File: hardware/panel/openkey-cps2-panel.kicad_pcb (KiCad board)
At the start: 2 copper layers, 124 x 108.8 mm, 198 parts, among them CN10 Conn_01x06, CN11 Conn_01x06, CN12 Conn_01x06, CN13 Conn_01x06, CN14 Conn_01x06, CN15 Conn_01x06, CN16 Conn_01x06, CN17 Conn_01x06, CN9 Conn_01x06, J1 VCC Pad, J10 VCC, J11 GND, J12 J5 / UDPI, J13 VCC Pad, J14 CN2, J15 GND Pad, J16 VCC, J17 GND, J18 J5 / UDPI, J19 VCC Pad, J2 CN2, J20 CN2, J21 GND Pad, J22 VCC, J23 GND, J24 J5 / UDPI, J25 VCC Pad, J26 CN2, J27 GND Pad, J28 VCC, J29 GND, J3 GND Pad, J30 J5 / UDPI, J31 VCC Pad, J32 CN2, J33 GND Pad, J34 VCC, J35 GND, J36 J5 / UDPI, J37 VCC Pad, J38 CN2, J39 GND Pad, J4 VCC, J40 VCC, J41 GND, J42 J5 / UDPI, J43 VCC Pad, J44 CN2, J45 GND Pad, J46 VCC, J47 GND, J48 J5 / UDPI, J49 VCC Pad, J5 GND, J50 CN2, J51 GND Pad, J52 VCC, J53 GND, J54 J5 / UDPI, J6 J5 / UDPI, J7 VCC Pad, J8 CN2, J9 GND Pad, U1 ATtinyxx4, U2 ATtinyxx4, U3 ATtinyxx4, U4 ATtinyxx4, U5 ATtinyxx4, U6 ATtinyxx4, U7 ATtinyxx4, U8 ATtinyxx4, U9 ATtinyxx4

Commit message: HW: bypass cap value typo'd as 100uf when it should be 100nf
Thanks for hatmoose for pointing out the typo
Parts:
- C1, C2, C3, C4, C5, C6, C7, C8, C9: value 100uf -> 100nf
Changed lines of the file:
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@@
     )
   )
-  (property "REV" "2022-12-17")
+  (property "REV" "2023-01-03")
   (net 0 "")
   (net 1 "VCC")
@@
       (effects (font (size 0.7 0.7) (thickness 0.12)))
     )
-    (fp_text value "100uf" (at -2.5 0) (layer "F.SilkS")
+    (fp_text value "100nf" (at -2.5 0) (layer "F.SilkS")
       (effects (font (size 0.7 0.7) (thickness 0.12)))
     )
@@
       (effects (font (size 0.7 0.7) (thickness 0.12)))
     )
-    (fp_text value "100uf" (at -2.5 0) (layer "F.SilkS")
+    (fp_text value "100nf" (at -2.5 0) (layer "F.SilkS")
       (effects (font (size 0.7 0.7) (thickness 0.12)))
     )
@@
       (effects (font (size 0.7 0.7) (thickness 0.12)))
     )
-    (fp_text value "100uf" (at -2.5 0) (layer "F.SilkS")
+    (fp_text value "100nf" (at -2.5 0) (layer "F.SilkS")
       (effects (font (size 0.7 0.7) (thickness 0.12)))
     )
@@
       (effects (font (size 0.7 0.7) (thickness 0.12)))
     )
-    (fp_text value "100uf" (at -2.5 0) (layer "F.SilkS")
+    (fp_text value "100nf" (at -2.5 0) (layer "F.SilkS")
       (effects (font (size 0.7 0.7) (thickness 0.12)))
     )
@@
       (effects (font (size 0.7 0.7) (thickness 0.12)))
     )
-    (fp_text value "100uf" (at -2.5 0) (layer "F.SilkS")
+    (fp_text value "100nf" (at -2.5 0) (layer "F.SilkS")
       (effects (font (size 0.7 0.7) (thickness 0.12)))
     )
@@
       (effects (font (size 0.7 0.7) (thickness 0.12)))
     )
-    (fp_text value "100uf" (at -2.5 0) (layer "F.SilkS")
+    (fp_text value "100nf" (at -2.5 0) (layer "F.SilkS")
       (effects (font (size 0.7 0.7) (thickness 0.12)))
     )
@@
       (effects (font (size 0.7 0.7) (thickness 0.12)))
     )
-    (fp_text value "100uf" (at -2.5 0) (layer "F.SilkS")
+    (fp_text value "100nf" (at -2.5 0) (layer "F.SilkS")
       (effects (font (size 0.7 0.7) (thickness 0.12)))
     )
@@
       (effects (font (size 0.7 0.7) (thickness 0.12)))
     )
-    (fp_text value "100uf" (at -2.5 0) (layer "F.SilkS")
+    (fp_text value "100nf" (at -2.5 0) (layer "F.SilkS")
       (effects (font (size 0.7 0.7) (thickness 0.12)))
     )
@@
       (effects (font (size 0.7 0.7) (thickness 0.12)))
     )
-    (fp_text value "100uf" (at -2.5 0) (layer "F.SilkS")
+    (fp_text value "100nf" (at -2.5 0) (layer "F.SilkS")
       (effects (font (size 0.7 0.7) (thickness 0.12)))
     )

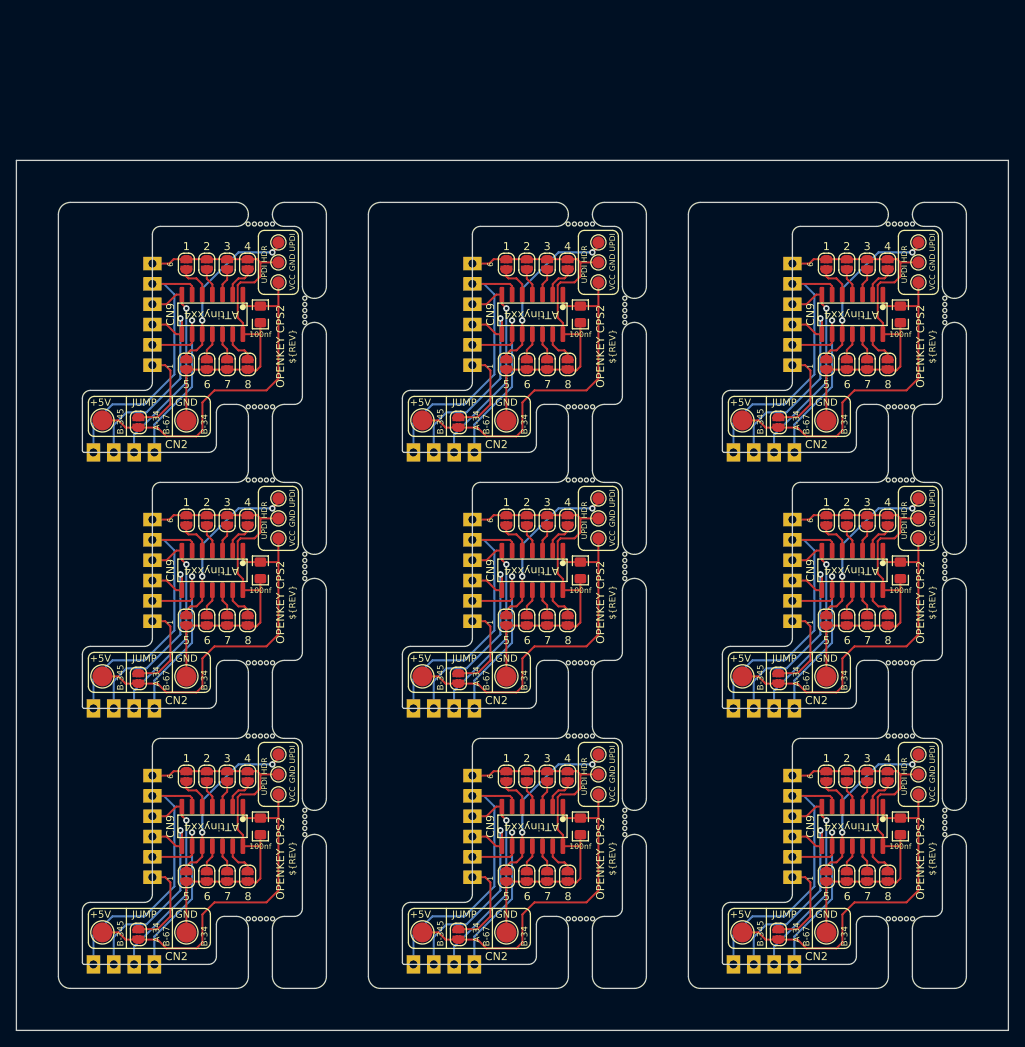
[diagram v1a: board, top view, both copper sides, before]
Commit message: panel + assembly updates
- have kikit create the panel (was done by hand before)
- have jlcpcb fabrication plugin create bom/positions files for the panel
- create PANEL.md with instructions for having jlcpcb assemble the board
- update kicad files to 10.x
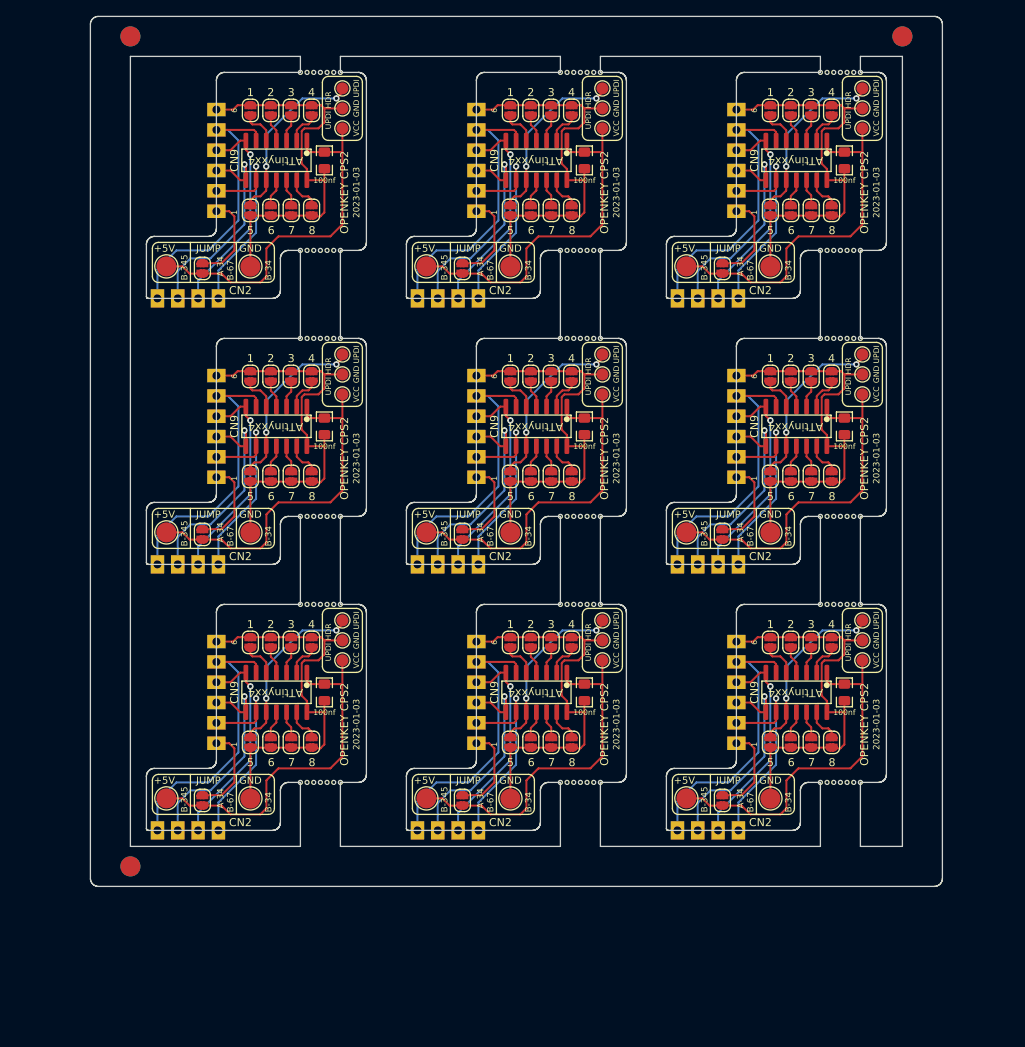
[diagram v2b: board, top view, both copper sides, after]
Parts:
- removed the C1 at (116.5, 57.2)
- removed C2, C3, C4, C5, C6, C7, C8, C9: 100nf, openkey:C_0805_2012Metric_Pad1.18x1.45mm_HandSolder
- removed CN10, CN11, CN12, CN13, CN14, CN15, CN16, CN17: Conn_01x06, Connector_PinHeader_2.54mm:PinHeader_1x06_P2.54mm_Vertical
- removed the CN9 at (103.0, 63.6)
- removed the J1 at (96.8, 70.5)
- removed J10, J16, J22, J28, J34, J40, J46, J52: VCC, TestPoint:TestPoint_Pad_D1.5mm
- removed J11, J17, J23, J29, J35, J41, J47, J53: GND, TestPoint:TestPoint_Pad_D1.5mm
- removed J12, J18, J24, J30, J36, J42, J48, J54: J5 / UDPI, TestPoint:TestPoint_Pad_D1.5mm
- removed J13, J19, J25, J31, J37, J43, J49, J7: VCC Pad, TestPoint:TestPoint_Pad_D2.5mm
- removed J14, J20, J26, J32, J38, J44, J50, J8: CN2, Connector_PinHeader_2.54mm:PinHeader_1x04_P2.54mm_Vertical
- removed J15, J21, J27, J33, J39, J45, J51, J9: GND Pad, TestPoint:TestPoint_Pad_D2.5mm
- removed the J2 at (103.2, 74.5)
- removed the J3 at (107.2, 70.5)
- removed the J4 at (118.8, 53.2)
- removed the J5 at (118.8, 50.8)
- removed the J6 at (118.8, 48.2)
- removed the JP1 at (107.2, 63.5)
- removed JP10, JP11, JP12, JP13, JP14, JP15, JP16, JP17, JP19, JP20, JP21, JP22, JP23, JP24, JP25, JP26, JP28, JP29, JP30, JP31, JP32, JP33, JP34, JP35, JP37, JP38, JP39, JP40, JP41, JP42, JP43, JP44, JP46, JP47, JP48, JP49, JP50, JP51, JP52, JP53, JP55, JP56, JP57, JP58, JP59, JP60, JP61, JP62, JP64, JP65, JP66, JP67, JP68, JP69, JP70, JP71, JP73, JP74, JP75, JP76, JP77, JP78, JP79, JP80: SolderJumper_2_Open, Jumper:SolderJumper-2_P1.3mm_Open_RoundedPad1.0x1.5mm
- removed JP18, JP27, JP36, JP45, JP54, JP63, JP72, JP81: CN9 VCC Jumper, Jumper:SolderJumper-2_P1.3mm_Open_RoundedPad1.0x1.5mm
- removed the JP2 at (109.8, 63.5)
- removed the JP3 at (112.3, 63.5)
- removed the JP4 at (114.9, 63.5)
- removed the JP5 at (114.9, 51.0)
- removed the JP6 at (112.3, 51.0)
- removed the JP7 at (109.8, 51.0)
- removed the JP8 at (107.2, 51.0)
- removed the JP9 at (101.2, 70.8)
- removed the REF** at (113.0, 58.0)
- removed REF**1, REF**2, REF**3, REF**4, REF**5, REF**6, REF**7, REF**8: OSHW-Logo_11.4x12mm_SilkScreen, Symbol:OSHW-Logo_11.4x12mm_SilkScreen
- removed the U1 at (110.5, 57.2)
- removed U2, U3, U4, U5, U6, U7, U8, U9: ATtinyxx4, openkey:SOIC-14_3.9x8.7mm_P1.27mm
- removed mouse-bite-3mm-slot1 (x3), mouse-bite-3mm-slot10, mouse-bite-3mm-slot11, mouse-bite-3mm-slot12, mouse-bite-3mm-slot13, mouse-bite-3mm-slot14, mouse-bite-3mm-slot15, mouse-bite-3mm-slot16, mouse-bite-3mm-slot17, mouse-bite-3mm-slot18, mouse-bite-3mm-slot19, mouse-bite-3mm-slot2, mouse-bite-3mm-slot20, mouse-bite-3mm-slot21, mouse-bite-3mm-slot22, mouse-bite-3mm-slot23, mouse-bite-3mm-slot24, mouse-bite-3mm-slot25, mouse-bite-3mm-slot3, mouse-bite-3mm-slot4, mouse-bite-3mm-slot5, mouse-bite-3mm-slot6, mouse-bite-3mm-slot7, mouse-bite-3mm-slot8, mouse-bite-3mm-slot9: VAL**, Panelization:mouse-bite-3mm-slot
- added C1: 100nf, openkey:C_0805_2012Metric_Pad1.18x1.45mm_HandSolder, F.Cu at (189.5, 71.2)
- added C1: 100nf, openkey:C_0805_2012Metric_Pad1.18x1.45mm_HandSolder, F.Cu at (124.5, 104.5)
- added C1: 100nf, openkey:C_0805_2012Metric_Pad1.18x1.45mm_HandSolder, F.Cu at (124.5, 71.2)
- added C1: 100nf, openkey:C_0805_2012Metric_Pad1.18x1.45mm_HandSolder, F.Cu at (189.5, 104.5)
- added C1: 100nf, openkey:C_0805_2012Metric_Pad1.18x1.45mm_HandSolder, F.Cu at (157.0, 71.2)
- added C1: 100nf, openkey:C_0805_2012Metric_Pad1.18x1.45mm_HandSolder, F.Cu at (157.0, 104.5)
- added C1: 100nf, openkey:C_0805_2012Metric_Pad1.18x1.45mm_HandSolder, F.Cu at (124.5, 38.0)
- added C1: 100nf, openkey:C_0805_2012Metric_Pad1.18x1.45mm_HandSolder, F.Cu at (157.0, 38.0)
- added C1: 100nf, openkey:C_0805_2012Metric_Pad1.18x1.45mm_HandSolder, F.Cu at (189.5, 38.0)
- added CN9: Conn_01x06, Connector_PinHeader_2.54mm:PinHeader_1x06_P2.54mm_Vertical, F.Cu at (176.0, 44.4)
- added CN9: Conn_01x06, Connector_PinHeader_2.54mm:PinHeader_1x06_P2.54mm_Vertical, F.Cu at (176.0, 77.6)
- added CN9: Conn_01x06, Connector_PinHeader_2.54mm:PinHeader_1x06_P2.54mm_Vertical, F.Cu at (143.5, 44.4)
- added CN9: Conn_01x06, Connector_PinHeader_2.54mm:PinHeader_1x06_P2.54mm_Vertical, F.Cu at (111.0, 110.8)
- added CN9: Conn_01x06, Connector_PinHeader_2.54mm:PinHeader_1x06_P2.54mm_Vertical, F.Cu at (143.5, 77.6)
- added CN9: Conn_01x06, Connector_PinHeader_2.54mm:PinHeader_1x06_P2.54mm_Vertical, F.Cu at (111.0, 44.4)
- added CN9: Conn_01x06, Connector_PinHeader_2.54mm:PinHeader_1x06_P2.54mm_Vertical, F.Cu at (143.5, 110.8)
- added CN9: Conn_01x06, Connector_PinHeader_2.54mm:PinHeader_1x06_P2.54mm_Vertical, F.Cu at (176.0, 110.8)
- added CN9: Conn_01x06, Connector_PinHeader_2.54mm:PinHeader_1x06_P2.54mm_Vertical, F.Cu at (111.0, 77.6)
- added J1: VCC Pad, TestPoint:TestPoint_Pad_D2.5mm, F.Cu at (104.8, 51.2)
- added J1: VCC Pad, TestPoint:TestPoint_Pad_D2.5mm, F.Cu at (169.8, 117.8)
- added J1: VCC Pad, TestPoint:TestPoint_Pad_D2.5mm, F.Cu at (137.2, 84.5)
- added J1: VCC Pad, TestPoint:TestPoint_Pad_D2.5mm, F.Cu at (104.8, 84.5)
- added J1: VCC Pad, TestPoint:TestPoint_Pad_D2.5mm, F.Cu at (137.2, 51.2)
- added J1: VCC Pad, TestPoint:TestPoint_Pad_D2.5mm, F.Cu at (169.8, 51.2)
- added J1: VCC Pad, TestPoint:TestPoint_Pad_D2.5mm, F.Cu at (169.8, 84.5)
- added J1: VCC Pad, TestPoint:TestPoint_Pad_D2.5mm, F.Cu at (104.8, 117.8)
- added J1: VCC Pad, TestPoint:TestPoint_Pad_D2.5mm, F.Cu at (137.2, 117.8)
- added J2: CN2, Connector_PinHeader_2.54mm:PinHeader_1x04_P2.54mm_Vertical, F.Cu at (143.8, 88.5)
- added J2: CN2, Connector_PinHeader_2.54mm:PinHeader_1x04_P2.54mm_Vertical, F.Cu at (176.2, 121.8)
- added J2: CN2, Connector_PinHeader_2.54mm:PinHeader_1x04_P2.54mm_Vertical, F.Cu at (143.8, 55.2)
- added J2: CN2, Connector_PinHeader_2.54mm:PinHeader_1x04_P2.54mm_Vertical, F.Cu at (111.2, 55.2)
- added J2: CN2, Connector_PinHeader_2.54mm:PinHeader_1x04_P2.54mm_Vertical, F.Cu at (111.2, 121.8)
- added J2: CN2, Connector_PinHeader_2.54mm:PinHeader_1x04_P2.54mm_Vertical, F.Cu at (176.2, 88.5)
- added J2: CN2, Connector_PinHeader_2.54mm:PinHeader_1x04_P2.54mm_Vertical, F.Cu at (176.2, 55.2)
- added J2: CN2, Connector_PinHeader_2.54mm:PinHeader_1x04_P2.54mm_Vertical, F.Cu at (111.2, 88.5)
- added J2: CN2, Connector_PinHeader_2.54mm:PinHeader_1x04_P2.54mm_Vertical, F.Cu at (143.8, 121.8)
- added J3: GND Pad, TestPoint:TestPoint_Pad_D2.5mm, F.Cu at (115.2, 84.5)
- added J3: GND Pad, TestPoint:TestPoint_Pad_D2.5mm, F.Cu at (115.2, 51.2)
- added J3: GND Pad, TestPoint:TestPoint_Pad_D2.5mm, F.Cu at (147.8, 84.5)
- added J3: GND Pad, TestPoint:TestPoint_Pad_D2.5mm, F.Cu at (180.2, 51.2)
- added J3: GND Pad, TestPoint:TestPoint_Pad_D2.5mm, F.Cu at (115.2, 117.8)
- added J3: GND Pad, TestPoint:TestPoint_Pad_D2.5mm, F.Cu at (147.8, 117.8)
- added J3: GND Pad, TestPoint:TestPoint_Pad_D2.5mm, F.Cu at (180.2, 117.8)
- added J3: GND Pad, TestPoint:TestPoint_Pad_D2.5mm, F.Cu at (147.8, 51.2)
- added J3: GND Pad, TestPoint:TestPoint_Pad_D2.5mm, F.Cu at (180.2, 84.5)
- added J4: VCC, TestPoint:TestPoint_Pad_D1.5mm, F.Cu at (159.2, 34.0)
- added J4: VCC, TestPoint:TestPoint_Pad_D1.5mm, F.Cu at (126.8, 100.5)
- added J4: VCC, TestPoint:TestPoint_Pad_D1.5mm, F.Cu at (126.8, 67.2)
- added J4: VCC, TestPoint:TestPoint_Pad_D1.5mm, F.Cu at (159.2, 100.5)
- added J4: VCC, TestPoint:TestPoint_Pad_D1.5mm, F.Cu at (191.8, 34.0)
- added J4: VCC, TestPoint:TestPoint_Pad_D1.5mm, F.Cu at (191.8, 100.5)
- added J4: VCC, TestPoint:TestPoint_Pad_D1.5mm, F.Cu at (191.8, 67.2)
- added J4: VCC, TestPoint:TestPoint_Pad_D1.5mm, F.Cu at (159.2, 67.2)
- added J4: VCC, TestPoint:TestPoint_Pad_D1.5mm, F.Cu at (126.8, 34.0)
- added J5: GND, TestPoint:TestPoint_Pad_D1.5mm, F.Cu at (126.8, 64.8)
- added J5: GND, TestPoint:TestPoint_Pad_D1.5mm, F.Cu at (126.8, 98.0)
- added J5: GND, TestPoint:TestPoint_Pad_D1.5mm, F.Cu at (191.8, 31.5)
- added J5: GND, TestPoint:TestPoint_Pad_D1.5mm, F.Cu at (191.8, 98.0)
- added J5: GND, TestPoint:TestPoint_Pad_D1.5mm, F.Cu at (159.2, 64.8)
- added J5: GND, TestPoint:TestPoint_Pad_D1.5mm, F.Cu at (159.2, 31.5)
- added J5: GND, TestPoint:TestPoint_Pad_D1.5mm, F.Cu at (126.8, 31.5)
- added J5: GND, TestPoint:TestPoint_Pad_D1.5mm, F.Cu at (159.2, 98.0)
- added J5: GND, TestPoint:TestPoint_Pad_D1.5mm, F.Cu at (191.8, 64.8)
- added J6: J5 / UDPI, TestPoint:TestPoint_Pad_D1.5mm, F.Cu at (191.8, 29.0)
- added J6: J5 / UDPI, TestPoint:TestPoint_Pad_D1.5mm, F.Cu at (159.2, 29.0)
- added J6: J5 / UDPI, TestPoint:TestPoint_Pad_D1.5mm, F.Cu at (126.8, 62.2)
- added J6: J5 / UDPI, TestPoint:TestPoint_Pad_D1.5mm, F.Cu at (191.8, 62.2)
- added J6: J5 / UDPI, TestPoint:TestPoint_Pad_D1.5mm, F.Cu at (126.8, 29.0)
- added J6: J5 / UDPI, TestPoint:TestPoint_Pad_D1.5mm, F.Cu at (159.2, 62.2)
- added J6: J5 / UDPI, TestPoint:TestPoint_Pad_D1.5mm, F.Cu at (126.8, 95.5)
- added J6: J5 / UDPI, TestPoint:TestPoint_Pad_D1.5mm, F.Cu at (191.8, 95.5)
- added J6: J5 / UDPI, TestPoint:TestPoint_Pad_D1.5mm, F.Cu at (159.2, 95.5)
- added JP1: SolderJumper_2_Open, Jumper:SolderJumper-2_P1.3mm_Open_RoundedPad1.0x1.5mm, F.Cu at (115.2, 110.8)
- added JP1: SolderJumper_2_Open, Jumper:SolderJumper-2_P1.3mm_Open_RoundedPad1.0x1.5mm, F.Cu at (147.8, 77.5)
- added JP1: SolderJumper_2_Open, Jumper:SolderJumper-2_P1.3mm_Open_RoundedPad1.0x1.5mm, F.Cu at (147.8, 110.8)
- added JP1: SolderJumper_2_Open, Jumper:SolderJumper-2_P1.3mm_Open_RoundedPad1.0x1.5mm, F.Cu at (180.2, 44.2)
- added JP1: SolderJumper_2_Open, Jumper:SolderJumper-2_P1.3mm_Open_RoundedPad1.0x1.5mm, F.Cu at (115.2, 44.2)
- added JP1: SolderJumper_2_Open, Jumper:SolderJumper-2_P1.3mm_Open_RoundedPad1.0x1.5mm, F.Cu at (115.2, 77.5)
- added JP1: SolderJumper_2_Open, Jumper:SolderJumper-2_P1.3mm_Open_RoundedPad1.0x1.5mm, F.Cu at (180.2, 77.5)
- added JP1: SolderJumper_2_Open, Jumper:SolderJumper-2_P1.3mm_Open_RoundedPad1.0x1.5mm, F.Cu at (147.8, 44.2)
- added JP1: SolderJumper_2_Open, Jumper:SolderJumper-2_P1.3mm_Open_RoundedPad1.0x1.5mm, F.Cu at (180.2, 110.8)
- added JP2: SolderJumper_2_Open, Jumper:SolderJumper-2_P1.3mm_Open_RoundedPad1.0x1.5mm, F.Cu at (150.3, 110.8)
- added JP2: SolderJumper_2_Open, Jumper:SolderJumper-2_P1.3mm_Open_RoundedPad1.0x1.5mm, F.Cu at (182.8, 77.5)
- added JP2: SolderJumper_2_Open, Jumper:SolderJumper-2_P1.3mm_Open_RoundedPad1.0x1.5mm, F.Cu at (150.3, 77.5)
- added JP2: SolderJumper_2_Open, Jumper:SolderJumper-2_P1.3mm_Open_RoundedPad1.0x1.5mm, F.Cu at (182.8, 110.8)
- added JP2: SolderJumper_2_Open, Jumper:SolderJumper-2_P1.3mm_Open_RoundedPad1.0x1.5mm, F.Cu at (150.3, 44.2)
- added JP2: SolderJumper_2_Open, Jumper:SolderJumper-2_P1.3mm_Open_RoundedPad1.0x1.5mm, F.Cu at (117.8, 77.5)
- added JP2: SolderJumper_2_Open, Jumper:SolderJumper-2_P1.3mm_Open_RoundedPad1.0x1.5mm, F.Cu at (182.8, 44.2)
- added JP2: SolderJumper_2_Open, Jumper:SolderJumper-2_P1.3mm_Open_RoundedPad1.0x1.5mm, F.Cu at (117.8, 110.8)
- added JP2: SolderJumper_2_Open, Jumper:SolderJumper-2_P1.3mm_Open_RoundedPad1.0x1.5mm, F.Cu at (117.8, 44.2)
- added JP3: SolderJumper_2_Open, Jumper:SolderJumper-2_P1.3mm_Open_RoundedPad1.0x1.5mm, F.Cu at (120.3, 110.8)
- added JP3: SolderJumper_2_Open, Jumper:SolderJumper-2_P1.3mm_Open_RoundedPad1.0x1.5mm, F.Cu at (185.3, 77.5)
- added JP3: SolderJumper_2_Open, Jumper:SolderJumper-2_P1.3mm_Open_RoundedPad1.0x1.5mm, F.Cu at (120.3, 44.2)
- added JP3: SolderJumper_2_Open, Jumper:SolderJumper-2_P1.3mm_Open_RoundedPad1.0x1.5mm, F.Cu at (152.8, 77.5)
- added JP3: SolderJumper_2_Open, Jumper:SolderJumper-2_P1.3mm_Open_RoundedPad1.0x1.5mm, F.Cu at (152.8, 110.8)
- added JP3: SolderJumper_2_Open, Jumper:SolderJumper-2_P1.3mm_Open_RoundedPad1.0x1.5mm, F.Cu at (152.8, 44.2)
- added JP3: SolderJumper_2_Open, Jumper:SolderJumper-2_P1.3mm_Open_RoundedPad1.0x1.5mm, F.Cu at (120.3, 77.5)
- added JP3: SolderJumper_2_Open, Jumper:SolderJumper-2_P1.3mm_Open_RoundedPad1.0x1.5mm, F.Cu at (185.3, 110.8)
- added JP3: SolderJumper_2_Open, Jumper:SolderJumper-2_P1.3mm_Open_RoundedPad1.0x1.5mm, F.Cu at (185.3, 44.2)
- added JP4: SolderJumper_2_Open, Jumper:SolderJumper-2_P1.3mm_Open_RoundedPad1.0x1.5mm, F.Cu at (155.4, 44.2)
- added JP4: SolderJumper_2_Open, Jumper:SolderJumper-2_P1.3mm_Open_RoundedPad1.0x1.5mm, F.Cu at (187.9, 110.8)
- added JP4: SolderJumper_2_Open, Jumper:SolderJumper-2_P1.3mm_Open_RoundedPad1.0x1.5mm, F.Cu at (155.4, 77.5)
- added JP4: SolderJumper_2_Open, Jumper:SolderJumper-2_P1.3mm_Open_RoundedPad1.0x1.5mm, F.Cu at (122.9, 110.8)
- added JP4: SolderJumper_2_Open, Jumper:SolderJumper-2_P1.3mm_Open_RoundedPad1.0x1.5mm, F.Cu at (122.9, 44.2)
- added JP4: SolderJumper_2_Open, Jumper:SolderJumper-2_P1.3mm_Open_RoundedPad1.0x1.5mm, F.Cu at (155.4, 110.8)
- added JP4: SolderJumper_2_Open, Jumper:SolderJumper-2_P1.3mm_Open_RoundedPad1.0x1.5mm, F.Cu at (187.9, 44.2)
- added JP4: SolderJumper_2_Open, Jumper:SolderJumper-2_P1.3mm_Open_RoundedPad1.0x1.5mm, F.Cu at (122.9, 77.5)
- added JP4: SolderJumper_2_Open, Jumper:SolderJumper-2_P1.3mm_Open_RoundedPad1.0x1.5mm, F.Cu at (187.9, 77.5)
- added JP5: SolderJumper_2_Open, Jumper:SolderJumper-2_P1.3mm_Open_RoundedPad1.0x1.5mm, F.Cu at (122.9, 65.0)
- added JP5: SolderJumper_2_Open, Jumper:SolderJumper-2_P1.3mm_Open_RoundedPad1.0x1.5mm, F.Cu at (187.9, 98.2)
- added JP5: SolderJumper_2_Open, Jumper:SolderJumper-2_P1.3mm_Open_RoundedPad1.0x1.5mm, F.Cu at (155.4, 98.2)
- added JP5: SolderJumper_2_Open, Jumper:SolderJumper-2_P1.3mm_Open_RoundedPad1.0x1.5mm, F.Cu at (187.9, 65.0)
- added JP5: SolderJumper_2_Open, Jumper:SolderJumper-2_P1.3mm_Open_RoundedPad1.0x1.5mm, F.Cu at (122.9, 31.8)
- added JP5: SolderJumper_2_Open, Jumper:SolderJumper-2_P1.3mm_Open_RoundedPad1.0x1.5mm, F.Cu at (155.4, 65.0)
- added JP5: SolderJumper_2_Open, Jumper:SolderJumper-2_P1.3mm_Open_RoundedPad1.0x1.5mm, F.Cu at (187.9, 31.8)
- added JP5: SolderJumper_2_Open, Jumper:SolderJumper-2_P1.3mm_Open_RoundedPad1.0x1.5mm, F.Cu at (122.9, 98.2)
- added JP5: SolderJumper_2_Open, Jumper:SolderJumper-2_P1.3mm_Open_RoundedPad1.0x1.5mm, F.Cu at (155.4, 31.8)
- added JP6: SolderJumper_2_Open, Jumper:SolderJumper-2_P1.3mm_Open_RoundedPad1.0x1.5mm, F.Cu at (185.3, 98.2)
- added JP6: SolderJumper_2_Open, Jumper:SolderJumper-2_P1.3mm_Open_RoundedPad1.0x1.5mm, F.Cu at (152.8, 31.8)
- added JP6: SolderJumper_2_Open, Jumper:SolderJumper-2_P1.3mm_Open_RoundedPad1.0x1.5mm, F.Cu at (185.3, 31.8)
- added JP6: SolderJumper_2_Open, Jumper:SolderJumper-2_P1.3mm_Open_RoundedPad1.0x1.5mm, F.Cu at (120.3, 65.0)
- added JP6: SolderJumper_2_Open, Jumper:SolderJumper-2_P1.3mm_Open_RoundedPad1.0x1.5mm, F.Cu at (185.3, 65.0)
- added JP6: SolderJumper_2_Open, Jumper:SolderJumper-2_P1.3mm_Open_RoundedPad1.0x1.5mm, F.Cu at (152.8, 98.2)
- added JP6: SolderJumper_2_Open, Jumper:SolderJumper-2_P1.3mm_Open_RoundedPad1.0x1.5mm, F.Cu at (120.3, 31.8)
- added JP6: SolderJumper_2_Open, Jumper:SolderJumper-2_P1.3mm_Open_RoundedPad1.0x1.5mm, F.Cu at (120.3, 98.2)
- added JP6: SolderJumper_2_Open, Jumper:SolderJumper-2_P1.3mm_Open_RoundedPad1.0x1.5mm, F.Cu at (152.8, 65.0)
- added JP7: SolderJumper_2_Open, Jumper:SolderJumper-2_P1.3mm_Open_RoundedPad1.0x1.5mm, F.Cu at (182.8, 98.2)
- added JP7: SolderJumper_2_Open, Jumper:SolderJumper-2_P1.3mm_Open_RoundedPad1.0x1.5mm, F.Cu at (150.3, 98.2)
- added JP7: SolderJumper_2_Open, Jumper:SolderJumper-2_P1.3mm_Open_RoundedPad1.0x1.5mm, F.Cu at (182.8, 65.0)
- added JP7: SolderJumper_2_Open, Jumper:SolderJumper-2_P1.3mm_Open_RoundedPad1.0x1.5mm, F.Cu at (150.3, 65.0)
- added JP7: SolderJumper_2_Open, Jumper:SolderJumper-2_P1.3mm_Open_RoundedPad1.0x1.5mm, F.Cu at (182.8, 31.8)
- added JP7: SolderJumper_2_Open, Jumper:SolderJumper-2_P1.3mm_Open_RoundedPad1.0x1.5mm, F.Cu at (117.8, 31.8)
- added JP7: SolderJumper_2_Open, Jumper:SolderJumper-2_P1.3mm_Open_RoundedPad1.0x1.5mm, F.Cu at (117.8, 98.2)
- added JP7: SolderJumper_2_Open, Jumper:SolderJumper-2_P1.3mm_Open_RoundedPad1.0x1.5mm, F.Cu at (150.3, 31.8)
- added JP7: SolderJumper_2_Open, Jumper:SolderJumper-2_P1.3mm_Open_RoundedPad1.0x1.5mm, F.Cu at (117.8, 65.0)
- added JP8: SolderJumper_2_Open, Jumper:SolderJumper-2_P1.3mm_Open_RoundedPad1.0x1.5mm, F.Cu at (147.8, 65.0)
- added JP8: SolderJumper_2_Open, Jumper:SolderJumper-2_P1.3mm_Open_RoundedPad1.0x1.5mm, F.Cu at (180.2, 65.0)
- added JP8: SolderJumper_2_Open, Jumper:SolderJumper-2_P1.3mm_Open_RoundedPad1.0x1.5mm, F.Cu at (115.2, 98.2)
- added JP8: SolderJumper_2_Open, Jumper:SolderJumper-2_P1.3mm_Open_RoundedPad1.0x1.5mm, F.Cu at (180.2, 31.8)
- added JP8: SolderJumper_2_Open, Jumper:SolderJumper-2_P1.3mm_Open_RoundedPad1.0x1.5mm, F.Cu at (115.2, 65.0)
- added JP8: SolderJumper_2_Open, Jumper:SolderJumper-2_P1.3mm_Open_RoundedPad1.0x1.5mm, F.Cu at (147.8, 98.2)
- added JP8: SolderJumper_2_Open, Jumper:SolderJumper-2_P1.3mm_Open_RoundedPad1.0x1.5mm, F.Cu at (180.2, 98.2)
- added JP8: SolderJumper_2_Open, Jumper:SolderJumper-2_P1.3mm_Open_RoundedPad1.0x1.5mm, F.Cu at (115.2, 31.8)
- added JP8: SolderJumper_2_Open, Jumper:SolderJumper-2_P1.3mm_Open_RoundedPad1.0x1.5mm, F.Cu at (147.8, 31.8)
- added JP9: CN9 VCC Jumper, Jumper:SolderJumper-2_P1.3mm_Open_RoundedPad1.0x1.5mm, F.Cu at (141.8, 118.0)
- added JP9: CN9 VCC Jumper, Jumper:SolderJumper-2_P1.3mm_Open_RoundedPad1.0x1.5mm, F.Cu at (109.2, 51.5)
- added JP9: CN9 VCC Jumper, Jumper:SolderJumper-2_P1.3mm_Open_RoundedPad1.0x1.5mm, F.Cu at (141.8, 84.8)
- added JP9: CN9 VCC Jumper, Jumper:SolderJumper-2_P1.3mm_Open_RoundedPad1.0x1.5mm, F.Cu at (174.2, 51.5)
- added JP9: CN9 VCC Jumper, Jumper:SolderJumper-2_P1.3mm_Open_RoundedPad1.0x1.5mm, F.Cu at (109.2, 84.8)
- added JP9: CN9 VCC Jumper, Jumper:SolderJumper-2_P1.3mm_Open_RoundedPad1.0x1.5mm, F.Cu at (141.8, 51.5)
- added JP9: CN9 VCC Jumper, Jumper:SolderJumper-2_P1.3mm_Open_RoundedPad1.0x1.5mm, F.Cu at (174.2, 118.0)
- added JP9: CN9 VCC Jumper, Jumper:SolderJumper-2_P1.3mm_Open_RoundedPad1.0x1.5mm, F.Cu at (174.2, 84.8)
- added JP9: CN9 VCC Jumper, Jumper:SolderJumper-2_P1.3mm_Open_RoundedPad1.0x1.5mm, F.Cu at (109.2, 118.0)
- added KiKit_FID_B_1: Fiducial, Fiducial, B.Cu at (100.2, 22.5)
- added KiKit_FID_B_2: Fiducial, Fiducial, B.Cu at (196.8, 22.5)
- added KiKit_FID_B_3: Fiducial, Fiducial, B.Cu at (100.2, 126.2)
- added KiKit_FID_T_1: Fiducial, Fiducial, F.Cu at (100.2, 22.5)
- added KiKit_FID_T_2: Fiducial, Fiducial, F.Cu at (196.8, 22.5)
- added KiKit_FID_T_3: Fiducial, Fiducial, F.Cu at (100.2, 126.2)
- added KiKit_MB_10_1: NPTH, NPTH, F.Cu at (154.0, 60.2)
- added KiKit_MB_10_2: NPTH, NPTH, F.Cu at (154.8, 60.2)
- added KiKit_MB_10_3: NPTH, NPTH, F.Cu at (155.7, 60.2)
- added KiKit_MB_10_4: NPTH, NPTH, F.Cu at (156.5, 60.2)
- added KiKit_MB_10_5: NPTH, NPTH, F.Cu at (157.3, 60.2)
- added KiKit_MB_10_6: NPTH, NPTH, F.Cu at (158.2, 60.2)
- added KiKit_MB_10_7: NPTH, NPTH, F.Cu at (159.0, 60.2)
- added KiKit_MB_11_1: NPTH, NPTH, F.Cu at (191.5, 82.5)
- added KiKit_MB_11_2: NPTH, NPTH, F.Cu at (190.7, 82.5)
- added KiKit_MB_11_3: NPTH, NPTH, F.Cu at (189.8, 82.5)
- added KiKit_MB_11_4: NPTH, NPTH, F.Cu at (189.0, 82.5)
- added KiKit_MB_11_5: NPTH, NPTH, F.Cu at (188.2, 82.5)
- added KiKit_MB_11_6: NPTH, NPTH, F.Cu at (187.3, 82.5)
- added KiKit_MB_11_7: NPTH, NPTH, F.Cu at (186.5, 82.5)
- added KiKit_MB_12_1: NPTH, NPTH, F.Cu at (186.5, 60.2)
- added KiKit_MB_12_2: NPTH, NPTH, F.Cu at (187.3, 60.2)
- added KiKit_MB_12_3: NPTH, NPTH, F.Cu at (188.2, 60.2)
- added KiKit_MB_12_4: NPTH, NPTH, F.Cu at (189.0, 60.2)
- added KiKit_MB_12_5: NPTH, NPTH, F.Cu at (189.8, 60.2)
- added KiKit_MB_12_6: NPTH, NPTH, F.Cu at (190.7, 60.2)
- added KiKit_MB_12_7: NPTH, NPTH, F.Cu at (191.5, 60.2)
- added KiKit_MB_13_1: NPTH, NPTH, F.Cu at (126.5, 115.8)
- added KiKit_MB_13_2: NPTH, NPTH, F.Cu at (125.7, 115.8)
- added KiKit_MB_13_3: NPTH, NPTH, F.Cu at (124.8, 115.8)
- added KiKit_MB_13_4: NPTH, NPTH, F.Cu at (124.0, 115.8)
- added KiKit_MB_13_5: NPTH, NPTH, F.Cu at (123.2, 115.8)
- added KiKit_MB_13_6: NPTH, NPTH, F.Cu at (122.3, 115.8)
- added KiKit_MB_13_7: NPTH, NPTH, F.Cu at (121.5, 115.8)
- added KiKit_MB_14_1: NPTH, NPTH, F.Cu at (121.5, 93.5)
- added KiKit_MB_14_2: NPTH, NPTH, F.Cu at (122.3, 93.5)
- added KiKit_MB_14_3: NPTH, NPTH, F.Cu at (123.2, 93.5)
- added KiKit_MB_14_4: NPTH, NPTH, F.Cu at (124.0, 93.5)
- added KiKit_MB_14_5: NPTH, NPTH, F.Cu at (124.8, 93.5)
- added KiKit_MB_14_6: NPTH, NPTH, F.Cu at (125.7, 93.5)
- added KiKit_MB_14_7: NPTH, NPTH, F.Cu at (126.5, 93.5)
- added KiKit_MB_15_1: NPTH, NPTH, F.Cu at (159.0, 115.8)
- added KiKit_MB_15_2: NPTH, NPTH, F.Cu at (158.2, 115.8)
- added KiKit_MB_15_3: NPTH, NPTH, F.Cu at (157.3, 115.8)
- added KiKit_MB_15_4: NPTH, NPTH, F.Cu at (156.5, 115.8)
- added KiKit_MB_15_5: NPTH, NPTH, F.Cu at (155.7, 115.8)
- added KiKit_MB_15_6: NPTH, NPTH, F.Cu at (154.8, 115.8)
- added KiKit_MB_15_7: NPTH, NPTH, F.Cu at (154.0, 115.8)
- added KiKit_MB_16_1: NPTH, NPTH, F.Cu at (154.0, 93.5)
- added KiKit_MB_16_2: NPTH, NPTH, F.Cu at (154.8, 93.5)
- added KiKit_MB_16_3: NPTH, NPTH, F.Cu at (155.7, 93.5)
- added KiKit_MB_16_4: NPTH, NPTH, F.Cu at (156.5, 93.5)
- added KiKit_MB_16_5: NPTH, NPTH, F.Cu at (157.3, 93.5)
- added KiKit_MB_16_6: NPTH, NPTH, F.Cu at (158.2, 93.5)
- added KiKit_MB_16_7: NPTH, NPTH, F.Cu at (159.0, 93.5)
- added KiKit_MB_17_1: NPTH, NPTH, F.Cu at (191.5, 115.8)
- added KiKit_MB_17_2: NPTH, NPTH, F.Cu at (190.7, 115.8)
- added KiKit_MB_17_3: NPTH, NPTH, F.Cu at (189.8, 115.8)
- added KiKit_MB_17_4: NPTH, NPTH, F.Cu at (189.0, 115.8)
- added KiKit_MB_17_5: NPTH, NPTH, F.Cu at (188.2, 115.8)
- added KiKit_MB_17_6: NPTH, NPTH, F.Cu at (187.3, 115.8)
- added KiKit_MB_17_7: NPTH, NPTH, F.Cu at (186.5, 115.8)
- added KiKit_MB_18_1: NPTH, NPTH, F.Cu at (186.5, 93.5)
- added KiKit_MB_18_2: NPTH, NPTH, F.Cu at (187.3, 93.5)
- added KiKit_MB_18_3: NPTH, NPTH, F.Cu at (188.2, 93.5)
- added KiKit_MB_18_4: NPTH, NPTH, F.Cu at (189.0, 93.5)
- added KiKit_MB_18_5: NPTH, NPTH, F.Cu at (189.8, 93.5)
- added KiKit_MB_18_6: NPTH, NPTH, F.Cu at (190.7, 93.5)
- added KiKit_MB_18_7: NPTH, NPTH, F.Cu at (191.5, 93.5)
- added KiKit_MB_1_1: NPTH, NPTH, F.Cu at (126.5, 49.2)
- added KiKit_MB_1_2: NPTH, NPTH, F.Cu at (125.7, 49.2)
- added KiKit_MB_1_3: NPTH, NPTH, F.Cu at (124.8, 49.2)
- added KiKit_MB_1_4: NPTH, NPTH, F.Cu at (124.0, 49.2)
- added KiKit_MB_1_5: NPTH, NPTH, F.Cu at (123.2, 49.2)
- added KiKit_MB_1_6: NPTH, NPTH, F.Cu at (122.3, 49.2)
- added KiKit_MB_1_7: NPTH, NPTH, F.Cu at (121.5, 49.2)
- added KiKit_MB_2_1: NPTH, NPTH, F.Cu at (121.5, 27.0)
- added KiKit_MB_2_2: NPTH, NPTH, F.Cu at (122.3, 27.0)
- added KiKit_MB_2_3: NPTH, NPTH, F.Cu at (123.2, 27.0)
- added KiKit_MB_2_4: NPTH, NPTH, F.Cu at (124.0, 27.0)
- added KiKit_MB_2_5: NPTH, NPTH, F.Cu at (124.8, 27.0)
- added KiKit_MB_2_6: NPTH, NPTH, F.Cu at (125.7, 27.0)
- added KiKit_MB_2_7: NPTH, NPTH, F.Cu at (126.5, 27.0)
- added KiKit_MB_3_1: NPTH, NPTH, F.Cu at (159.0, 49.2)
- added KiKit_MB_3_2: NPTH, NPTH, F.Cu at (158.2, 49.2)
- added KiKit_MB_3_3: NPTH, NPTH, F.Cu at (157.3, 49.2)
- added KiKit_MB_3_4: NPTH, NPTH, F.Cu at (156.5, 49.2)
- added KiKit_MB_3_5: NPTH, NPTH, F.Cu at (155.7, 49.2)
- added KiKit_MB_3_6: NPTH, NPTH, F.Cu at (154.8, 49.2)
- added KiKit_MB_3_7: NPTH, NPTH, F.Cu at (154.0, 49.2)
- added KiKit_MB_4_1: NPTH, NPTH, F.Cu at (154.0, 27.0)
- added KiKit_MB_4_2: NPTH, NPTH, F.Cu at (154.8, 27.0)
- added KiKit_MB_4_3: NPTH, NPTH, F.Cu at (155.7, 27.0)
- added KiKit_MB_4_4: NPTH, NPTH, F.Cu at (156.5, 27.0)
- added KiKit_MB_4_5: NPTH, NPTH, F.Cu at (157.3, 27.0)
- added KiKit_MB_4_6: NPTH, NPTH, F.Cu at (158.2, 27.0)
- added KiKit_MB_4_7: NPTH, NPTH, F.Cu at (159.0, 27.0)
- added KiKit_MB_5_1: NPTH, NPTH, F.Cu at (191.5, 49.2)
- added KiKit_MB_5_2: NPTH, NPTH, F.Cu at (190.7, 49.2)
- added KiKit_MB_5_3: NPTH, NPTH, F.Cu at (189.8, 49.2)
- added KiKit_MB_5_4: NPTH, NPTH, F.Cu at (189.0, 49.2)
- added KiKit_MB_5_5: NPTH, NPTH, F.Cu at (188.2, 49.2)
- added KiKit_MB_5_6: NPTH, NPTH, F.Cu at (187.3, 49.2)
- added KiKit_MB_5_7: NPTH, NPTH, F.Cu at (186.5, 49.2)
- added KiKit_MB_6_1: NPTH, NPTH, F.Cu at (186.5, 27.0)
- added KiKit_MB_6_2: NPTH, NPTH, F.Cu at (187.3, 27.0)
- added KiKit_MB_6_3: NPTH, NPTH, F.Cu at (188.2, 27.0)
- added KiKit_MB_6_4: NPTH, NPTH, F.Cu at (189.0, 27.0)
- added KiKit_MB_6_5: NPTH, NPTH, F.Cu at (189.8, 27.0)
- added KiKit_MB_6_6: NPTH, NPTH, F.Cu at (190.7, 27.0)
- added KiKit_MB_6_7: NPTH, NPTH, F.Cu at (191.5, 27.0)
- added KiKit_MB_7_1: NPTH, NPTH, F.Cu at (126.5, 82.5)
- added KiKit_MB_7_2: NPTH, NPTH, F.Cu at (125.7, 82.5)
- added KiKit_MB_7_3: NPTH, NPTH, F.Cu at (124.8, 82.5)
- added KiKit_MB_7_4: NPTH, NPTH, F.Cu at (124.0, 82.5)
- added KiKit_MB_7_5: NPTH, NPTH, F.Cu at (123.2, 82.5)
- added KiKit_MB_7_6: NPTH, NPTH, F.Cu at (122.3, 82.5)
- added KiKit_MB_7_7: NPTH, NPTH, F.Cu at (121.5, 82.5)
- added KiKit_MB_8_1: NPTH, NPTH, F.Cu at (121.5, 60.2)
- added KiKit_MB_8_2: NPTH, NPTH, F.Cu at (122.3, 60.2)
- added KiKit_MB_8_3: NPTH, NPTH, F.Cu at (123.2, 60.2)
- added KiKit_MB_8_4: NPTH, NPTH, F.Cu at (124.0, 60.2)
- added KiKit_MB_8_5: NPTH, NPTH, F.Cu at (124.8, 60.2)
- added KiKit_MB_8_6: NPTH, NPTH, F.Cu at (125.7, 60.2)
- added KiKit_MB_8_7: NPTH, NPTH, F.Cu at (126.5, 60.2)
- added KiKit_MB_9_1: NPTH, NPTH, F.Cu at (159.0, 82.5)
- added KiKit_MB_9_2: NPTH, NPTH, F.Cu at (158.2, 82.5)
- added KiKit_MB_9_3: NPTH, NPTH, F.Cu at (157.3, 82.5)
- added KiKit_MB_9_4: NPTH, NPTH, F.Cu at (156.5, 82.5)
- added KiKit_MB_9_5: NPTH, NPTH, F.Cu at (155.7, 82.5)
- added KiKit_MB_9_6: NPTH, NPTH, F.Cu at (154.8, 82.5)
- added KiKit_MB_9_7: NPTH, NPTH, F.Cu at (154.0, 82.5)
- added REF**: OSHW-Logo_11.4x12mm_SilkScreen, Symbol:OSHW-Logo_11.4x12mm_SilkScreen, B.Cu at (153.5, 72.0)
- added REF**: OSHW-Logo_11.4x12mm_SilkScreen, Symbol:OSHW-Logo_11.4x12mm_SilkScreen, B.Cu at (186.0, 38.8)
- added REF**: OSHW-Logo_11.4x12mm_SilkScreen, Symbol:OSHW-Logo_11.4x12mm_SilkScreen, B.Cu at (121.0, 105.2)
- added REF**: OSHW-Logo_11.4x12mm_SilkScreen, Symbol:OSHW-Logo_11.4x12mm_SilkScreen, B.Cu at (186.0, 105.2)
- added REF**: OSHW-Logo_11.4x12mm_SilkScreen, Symbol:OSHW-Logo_11.4x12mm_SilkScreen, B.Cu at (153.5, 105.2)
- added REF**: OSHW-Logo_11.4x12mm_SilkScreen, Symbol:OSHW-Logo_11.4x12mm_SilkScreen, B.Cu at (121.0, 38.8)
- added REF**: OSHW-Logo_11.4x12mm_SilkScreen, Symbol:OSHW-Logo_11.4x12mm_SilkScreen, B.Cu at (153.5, 38.8)
- added REF**: OSHW-Logo_11.4x12mm_SilkScreen, Symbol:OSHW-Logo_11.4x12mm_SilkScreen, B.Cu at (186.0, 72.0)
- added REF**: OSHW-Logo_11.4x12mm_SilkScreen, Symbol:OSHW-Logo_11.4x12mm_SilkScreen, B.Cu at (121.0, 72.0)
- added U1: ATtinyxx4, openkey:SOIC-14_3.9x8.7mm_P1.27mm, F.Cu at (183.5, 71.2)
- added U1: ATtinyxx4, openkey:SOIC-14_3.9x8.7mm_P1.27mm, F.Cu at (151.0, 104.5)
- added U1: ATtinyxx4, openkey:SOIC-14_3.9x8.7mm_P1.27mm, F.Cu at (183.5, 104.5)
- added U1: ATtinyxx4, openkey:SOIC-14_3.9x8.7mm_P1.27mm, F.Cu at (118.5, 38.0)
- added U1: ATtinyxx4, openkey:SOIC-14_3.9x8.7mm_P1.27mm, F.Cu at (151.0, 38.0)
- added U1: ATtinyxx4, openkey:SOIC-14_3.9x8.7mm_P1.27mm, F.Cu at (118.5, 104.5)
- added U1: ATtinyxx4, openkey:SOIC-14_3.9x8.7mm_P1.27mm, F.Cu at (183.5, 38.0)
- added U1: ATtinyxx4, openkey:SOIC-14_3.9x8.7mm_P1.27mm, F.Cu at (118.5, 71.2)
- added U1: ATtinyxx4, openkey:SOIC-14_3.9x8.7mm_P1.27mm, F.Cu at (151.0, 71.2)
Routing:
- net GND: track 459.0 -> 0.00 mm
- net VCC: track 409.9 -> 0.00 mm
- net RESET: track 318.1 -> 0.00 mm
- net SETUP: track 248.9 -> 0.00 mm, vias 9 -> 0
- net CLOCK: track 239.6 -> 0.00 mm, vias 9 -> 0
- net DATA: track 234.6 -> 0.00 mm, vias 9 -> 0
- net /J5 / UPDI: track 200.6 -> 0.00 mm, vias 18 -> 0
- net /CN9 VCC: track 101.8 -> 0.00 mm
- net Board_8-GND: track 0.00 -> 51.0 mm
- net Board_7-GND: track 0.00 -> 51.0 mm
- net Board_4-GND: track 0.00 -> 51.0 mm
- net Board_5-GND: track 0.00 -> 51.0 mm
- net Board_2-GND: track 0.00 -> 51.0 mm
- net Board_1-GND: track 0.00 -> 51.0 mm
- net Board_6-GND: track 0.00 -> 51.0 mm
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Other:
- board size 124 x 108.8 mm -> 106.5 x 108.8 mm
- board text added: "2023-01-03"
- board text added: "HW REV 2023-01-03"
- board text removed: "${REV}"
- board text removed: "HW REV ${REV}"
